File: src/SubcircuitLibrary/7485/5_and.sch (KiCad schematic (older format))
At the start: 4 parts, among them U1 PORT, U2 d_and, U3 d_and, X1 3_and

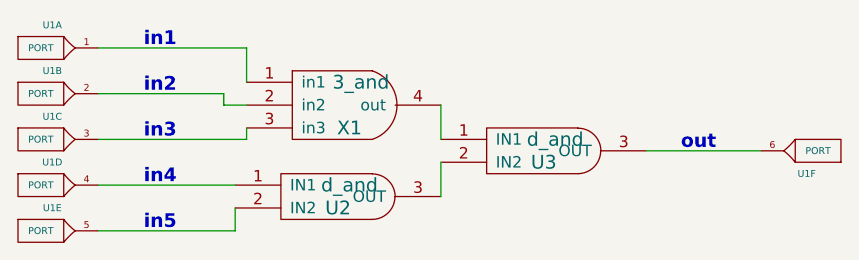
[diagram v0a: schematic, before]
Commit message: common code for Win and Linux, merged py2 changes
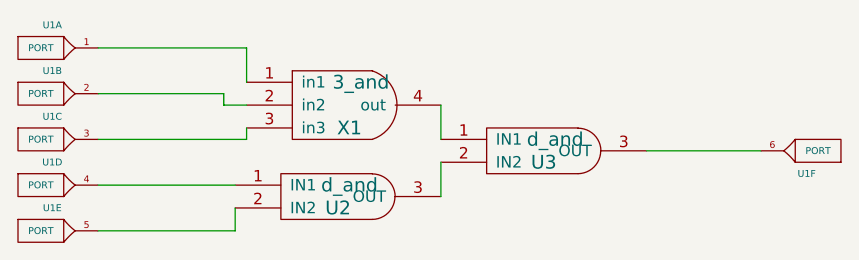
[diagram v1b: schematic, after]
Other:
- note removed: "in1"
- note removed: "in2"
- note removed: "in3"
- note removed: "in4"
- note removed: "in5"
- note removed: "out"
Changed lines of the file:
@@
 LIBS:eSim_Subckt
 LIBS:eSim_User
-LIBS:5_and-cache
 EELAYER 25 0
 EELAYER END
@@
 	-1   0    0    1
 $EndComp
-Text Notes 3800 2700 0    60   ~ 12
-in1
-Text Notes 3800 2900 0    60   ~ 12
-in2
-Text Notes 3800 3100 0    60   ~ 12
-in3
-Text Notes 3800 3300 0    60   ~ 12
-in4
-Text Notes 3800 3500 0    60   ~ 12
-in5
-Text Notes 6150 3150 0    60   ~ 12
-out
 $EndSCHEMATC
